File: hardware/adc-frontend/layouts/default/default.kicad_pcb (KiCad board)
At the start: 4 copper layers, 100.5 x 100 mm, 144 parts

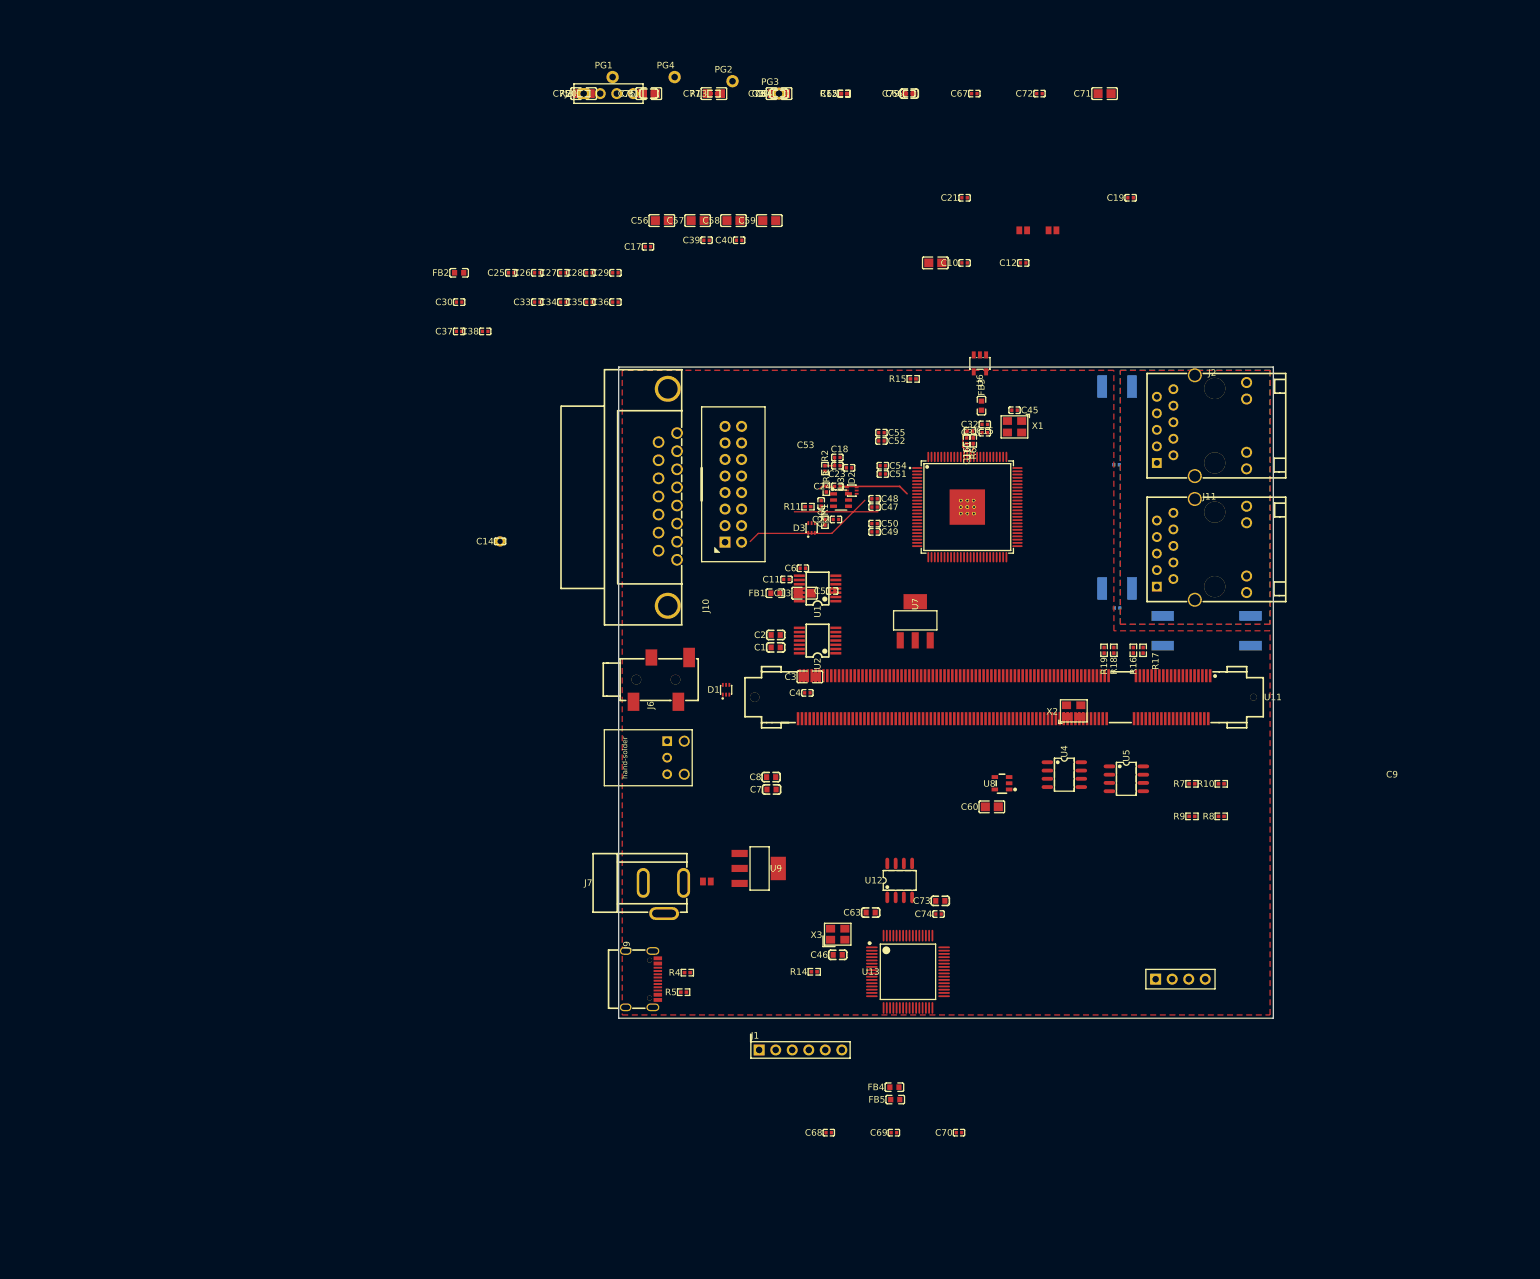
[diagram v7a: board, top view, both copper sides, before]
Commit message: デジタルRGB入力とデバッグ端子を追加し、SO-DIMMを寝かせ型の実部品へ差し替える
デジタルRGB入力(J13): PC-6001mkII/SR・PC-8801 等の TTL RGBI + HS/VS を、TVP7002 を
経由せず FPGA へ直結する。ドットクロックは FPGA 内のオーバーサンプリングで再生する
のでクロック線は持たない。ECP5 の I/O は 5V トレラントではないので、既存の同期
バッファと同じ SN74LVC2G17 (入力5.5V許容・シュミット) を dual×3=6ch で挟む
(同一型番なので BOM 行が増えない)。コネクタは 1.25mm 単列8極。8極では信号6本+GND2本
しか取れないため、フレームごと壊れる同期を GND 隣に置き、色4bitを中央にまとめた。
アナログ経路とは FPGA ピンが別なので、アナログ機とデジタル機を両方繋いだままにできる。

デバッグ端子(J4): SO-DIMM 偶数側 pin54〜94 が pin56(GND) を除いて完全に連続した
空き GPIO 20本だったので、2×15 ヘッダへ単調割当(交差無し)で引き出す。
dbg14 は J18 = GR_PCLK2_0 なので外部クロック入力にも使える。

SO-DIMM ソケット: 流用元の JST DM-7D4-H2500(M) はモジュールが垂直に立つタイプ
だった。本設計は JTAG をモジュール底面へポゴピンで当てる前提なので、寝かせ型で
なければ成立しない。TE 1473005-4 = LCSC C428482 のベンダ純正フットプリント
(ラッチ保持パッド・非対称位置決め穴・STEP付き)へ差し替えた。列間は 8.60mm。
途中 TE 仕様表の "Reihenabstand 6.2mm" を列間と誤読したが、実フットプリント3件が
いずれも 8.2〜8.6mm で、あれは基板ランドの列間ではない。

Ethernet LED: PHY の LED 出力をモジュール底面からバネ端子で拾う経路を足した
(PG5-8 → 220Ω → MagJack pin11/14)。ゲートウェア不要で、ビットストリームを焼く前から
リンク状態が光るので実機の切り分けに効く。従来の GPIO 経路も直列はんだジャンパ
(JP4-7, 既定=開)で残してあり、接触不良時に基板改造なしで戻せる。両方同時に生かすと
アノードで押し合うので、PHY 経路使用時はゲートウェアで GPIO を入力にしておく。

設計ルール: 0.5mmピッチQFPと0.6mmピッチSO-DIMMからファンアウトできなかったので、
JLCPCB 4層の実能力に合わせた。Default クリアランス 0.20→0.127mm、ビア
0.6/0.3→0.45/0.25mm (穴0.25/径0.45 が追加費用のかからない下限)、銅-基板外形
0.5→0.25mm。GbE は 0.4/0.6mm のままだと 0.6mmピッチのコネクタで線幅ゼロでも
満たせないため、U11 のパッド周りだけ 0.2mm に緩める規則を足した。条件式は
memberOfFootprint だけが実際にマッチする (memberOf / insideCourtyard は構文が
通るだけで何にもマッチしないので、極端な値を入れて発火を確認すること)。

その他:
- 取付穴が「穴径=パッド径のPTH」でアニュラー幅が負(-0.003mm)になっていた5部品を
  NPTH 化。樹脂ボスの位置決め穴なので非メッキが正しい
- TE ソケットに F.CrtYd を追加。コートヤード判定が効いていなかった
- docs: パスコン84個の配置先一覧(検索・優先度絞り込み・印刷可)を追加し、
  index から辿れるようにした。designator と役割は kicad_pcb の atopile_address
  から機械的に対応付けている

ato build 成功。pad→net 割当は全件照合済み。

Co-Authored-By: Claude Opus 5 (1M context) <noreply@anthropic.com>
Claude-Session: https://claude.ai/code/session_01AYX9RsES3rPuz5gJsqFGst
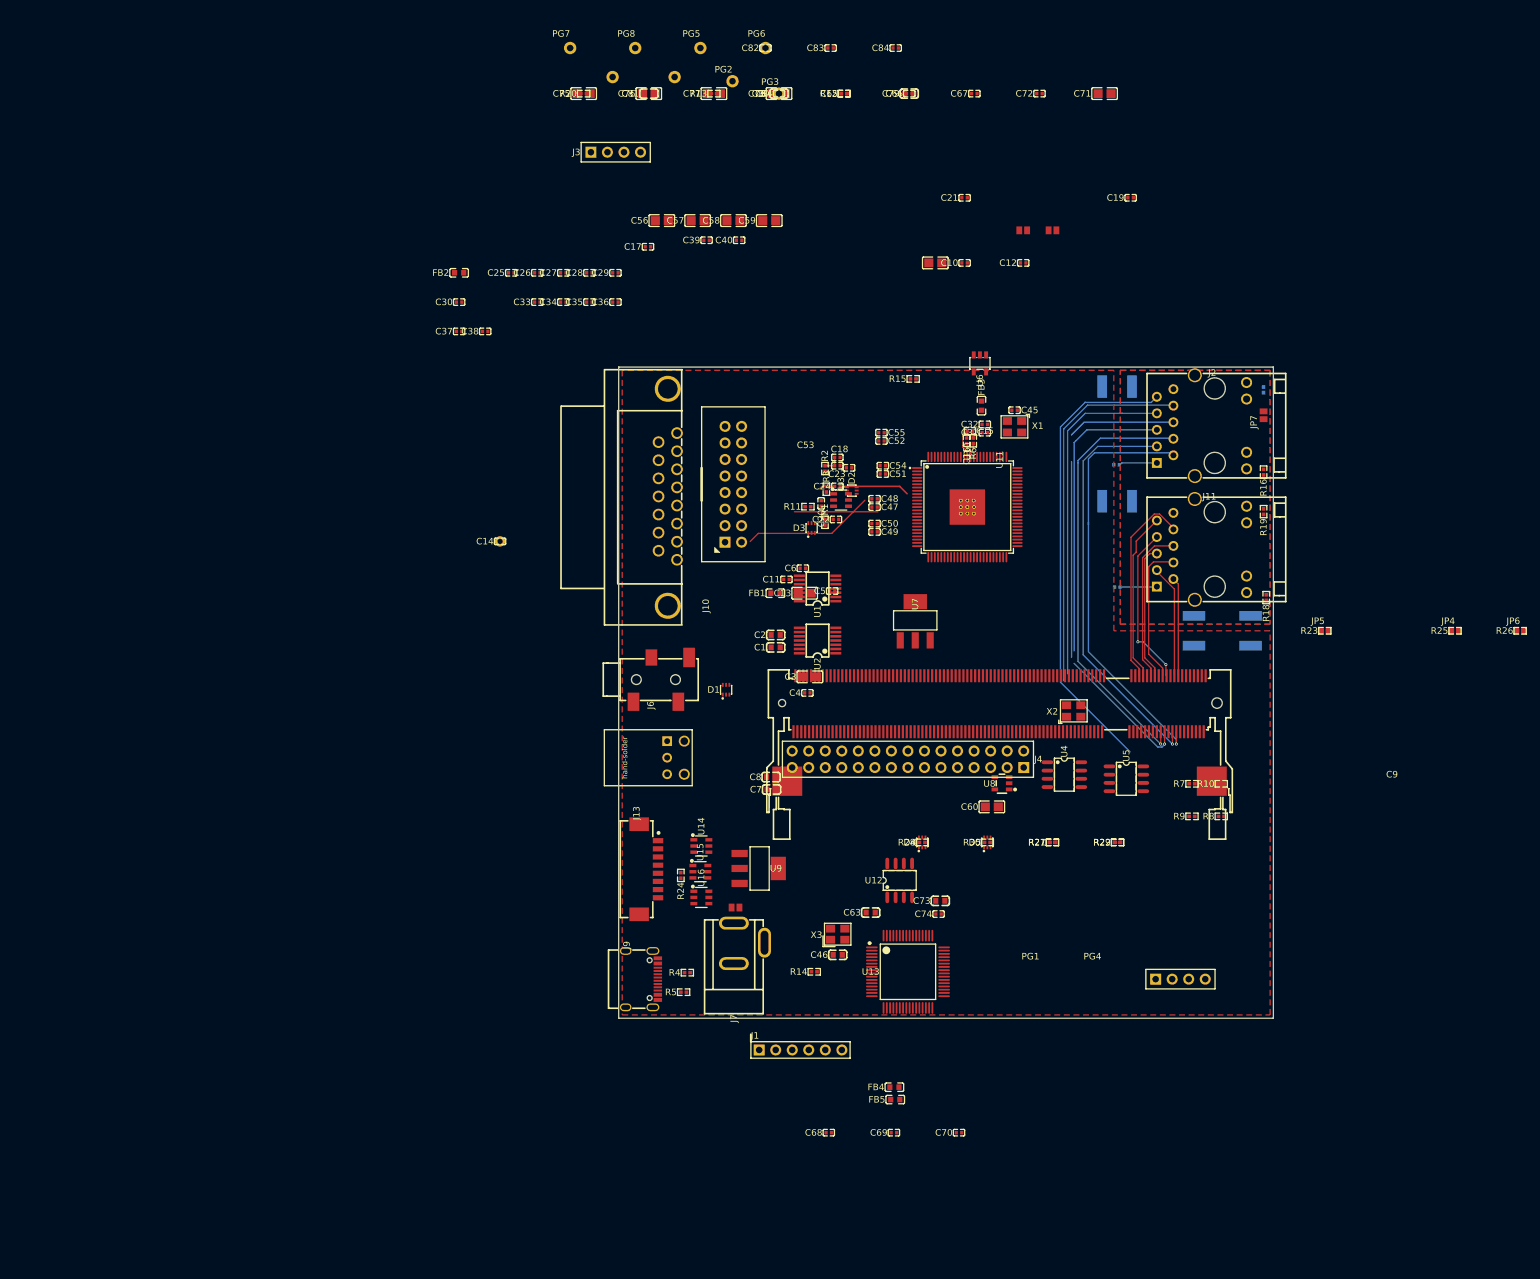
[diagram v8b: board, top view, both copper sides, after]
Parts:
- added C82: 100nF ±10%, SAMSUNG_CL05B104KO5NNNC:C0402, F.Cu at (110.0, 0.00)
- added C83: 100nF ±10%, SAMSUNG_CL05B104KO5NNNC:C0402, F.Cu at (120.0, 0.00)
- added C84: 100nF ±10%, SAMSUNG_CL05B104KO5NNNC:C0402, F.Cu at (130.0, 0.00)
- added D4: , ROHM_EMZT6_8ET2R:EMT6_L1.6-W1.2-P0.50-LS1.6-BL, F.Cu at (134.1, 122.0)
- added D5: , ROHM_EMZT6_8ET2R:EMT6_L1.6-W1.2-P0.50-LS1.6-BL, F.Cu at (144.1, 122.0)
- added J13: , YIYUAN_YTC_A1251_08ABW:CONN-SMD_8P-P1.25_YTC-A1251-08ABW, F.Cu at (92.0, 126.1)
- added J4: , _mech:Header_2x15_P2.54mm, F.Cu at (149.7, 110.5)
- added JP4: , _mech:SolderJumper_2, F.Cu at (215.9, 89.5)
- added JP5: , _mech:SolderJumper_2, F.Cu at (195.9, 89.5)
- added JP6: , _mech:SolderJumper_2, F.Cu at (225.9, 89.5)
- added JP7: , _mech:SolderJumper_2, F.Cu at (186.5, 56.4)
- added PG5: , _mech:PogoPin_D1.0mm, F.Cu at (100.0, 0.00)
- added PG6: , _mech:PogoPin_D1.0mm, F.Cu at (110.0, 0.00)
- added PG7: , _mech:PogoPin_D1.0mm, F.Cu at (80.0, 0.00)
- added PG8: , _mech:PogoPin_D1.0mm, F.Cu at (90.0, 0.00)
- added R21: 10kΩ ±1%, UNI_ROYAL_0402WGF1002TCE:R0402, F.Cu at (154.1, 122.0)
- added R22: 10kΩ ±1%, UNI_ROYAL_0402WGF1002TCE:R0402, F.Cu at (164.1, 122.0)
- added R23: 10kΩ ±1%, UNI_ROYAL_0402WGF1002TCE:R0402, F.Cu at (195.9, 89.5)
- added R24: 10kΩ ±1%, UNI_ROYAL_0402WGF1002TCE:R0402, F.Cu at (97.0, 127.1)
- added R25: 10kΩ ±1%, UNI_ROYAL_0402WGF1002TCE:R0402, F.Cu at (215.9, 89.5)
- added R26: 10kΩ ±1%, UNI_ROYAL_0402WGF1002TCE:R0402, F.Cu at (225.9, 89.5)
- added R27: 220Ω ±1%, UNI_ROYAL_0402WGF2200TCE:R0402, F.Cu at (154.1, 122.0)
- added R28: 220Ω ±1%, UNI_ROYAL_0402WGF2200TCE:R0402, F.Cu at (134.1, 122.0)
- added R29: 220Ω ±1%, UNI_ROYAL_0402WGF2200TCE:R0402, F.Cu at (164.1, 122.0)
- added R30: 220Ω ±1%, UNI_ROYAL_0402WGF2200TCE:R0402, F.Cu at (144.1, 122.0)
- added U14: , TI_SN74LVC2G17DBVR:SOT-23-6_L2.9-W1.6-P0.95-LS2.8-BL, F.Cu at (100.2, 122.5)
- added U15: , TI_SN74LVC2G17DBVR:SOT-23-6_L2.9-W1.6-P0.95-LS2.8-BL, F.Cu at (100.0, 126.5)
- added U16: , TI_SN74LVC2G17DBVR:SOT-23-6_L2.9-W1.6-P0.95-LS2.8-BL, F.Cu at (100.2, 130.4)
- R17: moved to B.Cu
- U11: footprint JST_DM_7D4_H2500_M:DIMM-SMD_DM-7D4-H2500-M -> TE_Connectivity_1473005_4:SO-DIMM-SMD_200P-P0.60_1473005-4
- moved R17 44.1 mm to (186.5, 52.5)
- moved R16 33.9 mm to (186.5, 65.1)
- moved R19 32.5 mm to (186.5, 71.2)
- moved R18 24.8 mm to (186.9, 84.4)
- moved J7 14.9 mm to (107.5, 137.5), turned to 90 degrees
- moved C41 13.4 mm to (164.0, 69.6)
- moved J3 9.07 mm to (83.2, 16.0)
- moved JP3 5.95 mm to (105.4, 132.0)
- moved U11 4.85 mm to (145.9, 104.5), turned to -90 degrees
- moved C61 4.80 mm to (175.8, 89.5)
- moved C44 3.20 mm to (164.0, 82.8)
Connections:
- net 4 renamed esd_sync-4
- net 6 renamed esd_rgb-6
- net eth-led_g_a renamed eth1_led_g_anode
- net eth-led_y_a renamed eth1_led_y_anode
- net led_g_a renamed eth2_led_g_anode
- net led_y_a renamed eth2_led_y_anode
- R16 pad 1: eth2_led_g -> eth2_led_g_gpio_sj
- R17 pad 1: eth2_led_y -> eth2_led_y_gpio_sj
- R18 pad 1: eth1_led_g -> eth1_led_g_gpio_sj
- R19 pad 1: eth1_led_y -> eth1_led_y_gpio_sj
- U11 pad 132: 132 -> drgb_hs
- U11 pad 136: 136 -> drgb_r
- U11 pad 140: 140 -> drgb_g
- U11 pad 142: 142 -> drgb_b
- U11 pad 144: 144 -> drgb_i
- U11 pad 146: 146 -> drgb_vs
- U11 pad 42: eth2_led_g -> eth2_led_g_gpio
- U11 pad 44: eth2_led_y -> eth2_led_y_gpio
- U11 pad 46: eth1_led_g -> eth1_led_g_gpio
- U11 pad 48: eth1_led_y -> eth1_led_y_gpio
- U11 pad 54: (no net) -> dbg01_m1
- U11 pad 58: (no net) -> dbg02_n2
- U11 pad 60: (no net) -> dbg03_n3
- U11 pad 62: (no net) -> dbg04_t2
- U11 pad 64: (no net) -> dbg05_m3
- U11 pad 66: (no net) -> dbg06_t3
- U11 pad 68: (no net) -> dbg07_r3
- U11 pad 70: (no net) -> dbg08_n4
- U11 pad 72: (no net) -> dbg09_m4
- U11 pad 74: (no net) -> dbg10_l4
- U11 pad 76: (no net) -> dbg11_l5
- U11 pad 78: (no net) -> dbg12_p16
- U11 pad 80: (no net) -> dbg13_j16
- U11 pad 82: (no net) -> dbg14_j18_pclk
- U11 pad 84: (no net) -> dbg15_j17
- U11 pad 86: (no net) -> dbg16_h18
- U11 pad 88: (no net) -> dbg17_h17
- U11 pad 90: (no net) -> dbg18_g18
- U11 pad 92: (no net) -> dbg19_h16
- U11 pad 94: (no net) -> dbg20_f18
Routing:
- net eth2_2_N: track 0.00 -> 73.5 mm, vias 0 -> 1
- net eth2_4_N: track 0.00 -> 71.1 mm
- net eth2_2_P: track 0.00 -> 66.8 mm, vias 0 -> 1
- net eth2_1_P: track 0.00 -> 65.3 mm, vias 0 -> 1
- net eth2_1_N: track 0.00 -> 63.3 mm, vias 0 -> 1
- net eth2_4_P: track 0.00 -> 57.3 mm
- net eth2_3_N: track 0.00 -> 49.0 mm
- net eth2_3_P: track 0.00 -> 45.5 mm
- net eth1_4_P: track 0.00 -> 31.0 mm
- net eth1_4_N: track 0.00 -> 26.0 mm
- net eth1_2_N: track 0.00 -> 24.8 mm, vias 0 -> 2
- net eth1_3_N: track 0.00 -> 24.1 mm
- net eth1_2_P: track 0.00 -> 21.8 mm
- net eth1_3_P: track 0.00 -> 20.8 mm
- net eth1_1_N: track 0.00 -> 17.3 mm
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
